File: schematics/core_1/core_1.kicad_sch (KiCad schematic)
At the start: 27 parts, among them U1 74LS00, U2 74LS04, U3 74LS109, U4 74LS02

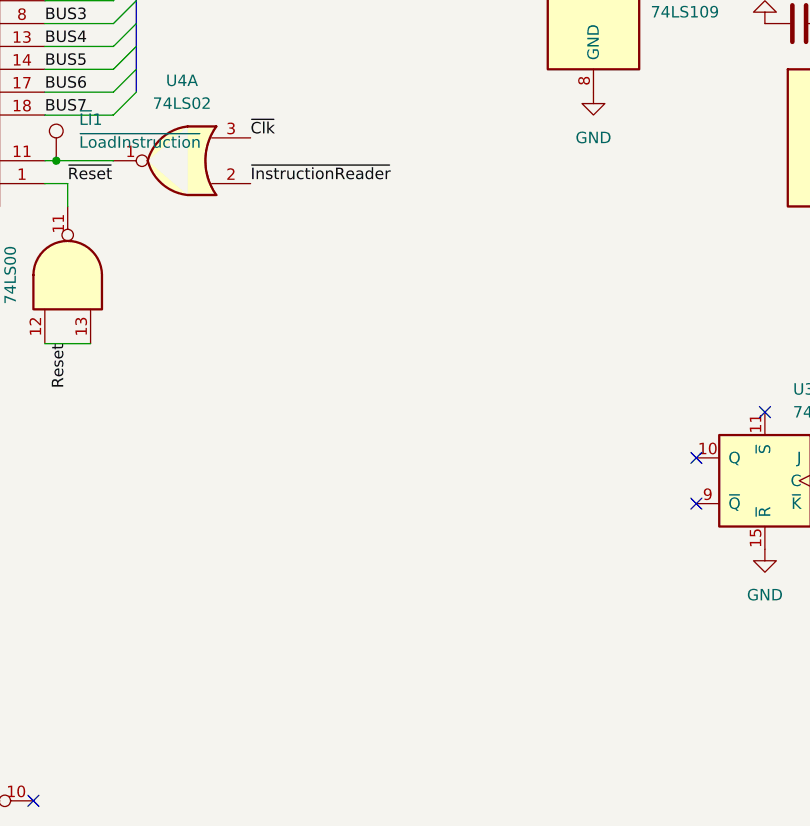
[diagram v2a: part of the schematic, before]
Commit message: Add hotfix for timing issue
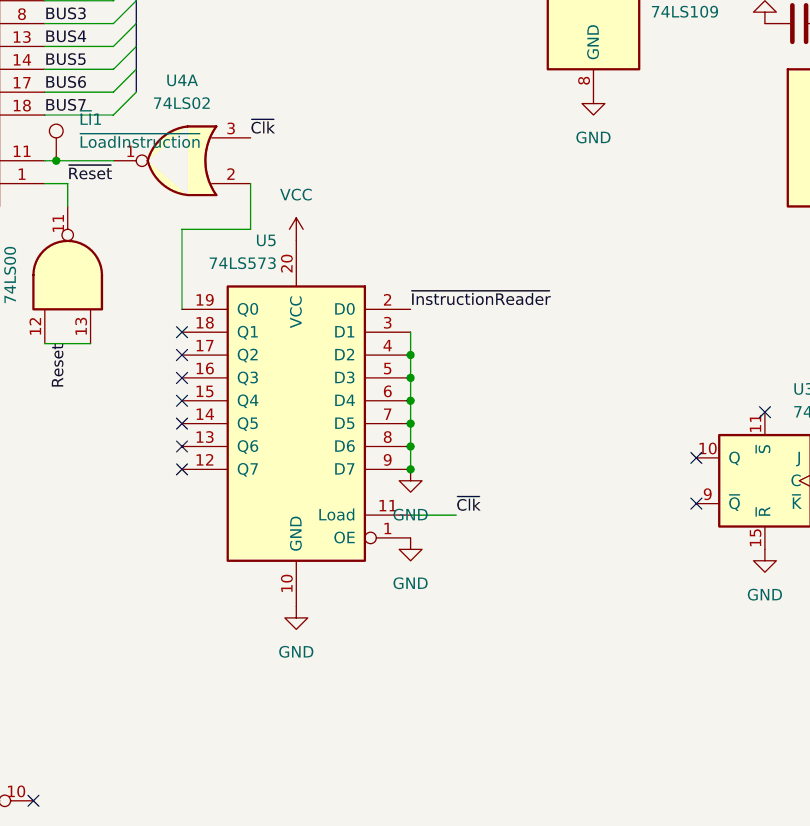
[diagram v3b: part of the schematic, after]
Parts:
- added U5: 74LS573, symbol 74xx:74LS573
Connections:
- net GND: now also U5.1 (OE), U5.10 (GND), U5.3 (D1), U5.4 (D2), U5.5 (D3), U5.6 (D4), U5.7 (D5), U5.8 (D6), U5.9 (D7)
- net VCC: now also U5.20 (VCC)
- net ~{Clk}: now also U5.11 (Load)
- net ~{InstructionReader}: now also U5.2 (D0); no longer U4.2
- new net: U4.2, U5.19 (Q0)
- no-connect marks 67 -> 74

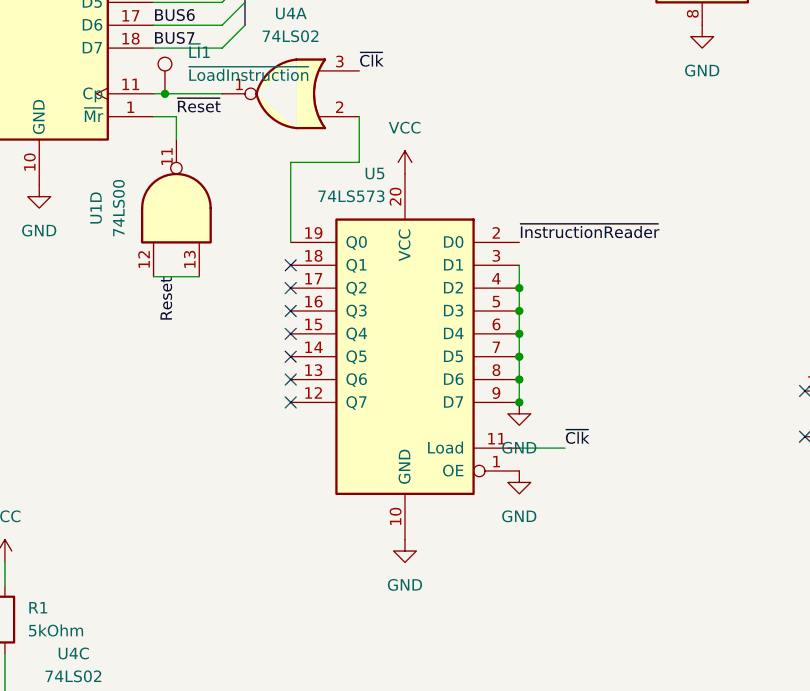
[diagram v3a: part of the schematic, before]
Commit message: Remake with ic74373
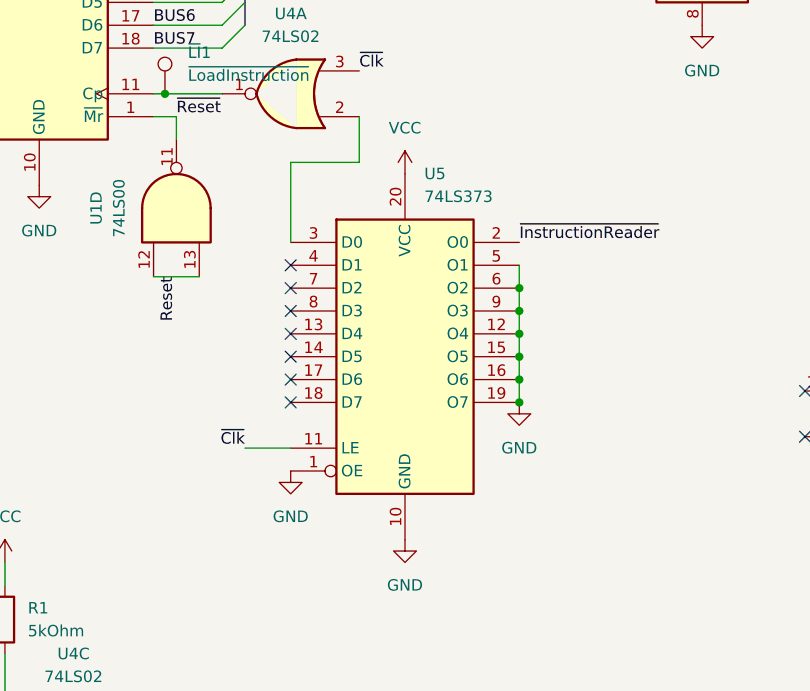
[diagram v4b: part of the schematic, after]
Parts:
- removed U5: 74LS573, symbol 74xx:74LS573
- added U5: 74LS373, symbol 74xx:74LS373
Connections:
- net GND: now also U5.1 (OE), U5.10 (GND), U5.12 (O4), U5.15 (O5), U5.16 (O6), U5.19 (O7), U5.5 (O1), U5.6 (O2), U5.9 (O3)
- net VCC: now also U5.20 (VCC)
- net ~{Clk}: now also U5.11 (LE)
- net ~{InstructionReader}: now also U5.2 (O0)
- net at U4.2: now also U5.3 (D0)
